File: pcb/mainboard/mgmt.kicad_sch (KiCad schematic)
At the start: 91 parts, among them J10 FAN_01, J11 XILINX_JTAG, J12 JUMPER_0402_SPDT, J13 JUMPER_0402_SPDT, J14 RJ45, J15 PMOD_HOST, J48 CONN_01X10, J8 FAN_01, J9 CONN_01X03, U23 STM32H735-UFBGA176-25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

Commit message: More work in supervisor region
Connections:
- net FAN1_TACH: now also U8.G22 (IO_L8N_T1_D12_14); no longer U8.J21 (IO_L10P_T1_D14_14)
- net FRONTPANEL_CS_N: now also U8.L21 (IO_L18N_T2_A11_D27_14); no longer U8.E21 (IO_L7P_T1_D09_14)
- net FRONTPANEL_MISO: now also U8.N22 (IO_L15P_T2_DQS_RDWR_B_14); no longer U8.H22 (IO_L8P_T1_D11_14)
- net FRONTPANEL_MOSI: now also U8.K21 (IO_L16P_T2_CSI_B_14); no longer U8.E22 (IO_L7N_T1_D10_14)
- net FRONTPANEL_SCK: now also U8.K22 (IO_L16N_T2_A15_D31_14); no longer U8.G22 (IO_L8N_T1_D12_14)
- net MCU_IRQ: now also U8.J21 (IO_L10P_T1_D14_14); no longer U8.M20 (IO_L18P_T2_A12_D28_14)
- net MCU_QSPI_CS_N: now also U8.H22 (IO_L8P_T1_D11_14); no longer U8.M21 (IO_L17N_T2_A13_D29_14)
- net MCU_QSPI_DQ0: now also U8.F20 (IO_L4N_T0_D05_14); no longer U8.L20 (IO_L12N_T1_MRCC_14)
- net MCU_QSPI_DQ1: now also U8.E22 (IO_L7N_T1_D10_14); no longer U8.N22 (IO_L15P_T2_DQS_RDWR_B_14)
- net MCU_QSPI_DQ2: now also U8.G20 (IO_L4P_T0_D04_14); no longer U8.K22 (IO_L16N_T2_A15_D31_14)
- net MCU_QSPI_DQ3: now also U8.F21 (IO_L9N_T1_DQS_D13_14); no longer U8.L21 (IO_L18N_T2_A11_D27_14)
- net MCU_QSPI_SCK: now also U8.E21 (IO_L7P_T1_D09_14); no longer U8.K21 (IO_L16P_T2_CSI_B_14)
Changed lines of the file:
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@@
   (no_connect (at 245.11 60.96))
   (no_connect (at 287.02 91.44))
+  (no_connect (at 354.33 81.28))
   (no_connect (at 280.67 71.12))
-  (no_connect (at 354.33 40.64))
   (no_connect (at 200.66 119.38))
   (no_connect (at 200.66 91.44))
@@
   (no_connect (at 245.11 45.72))
   (no_connect (at 245.11 119.38))
+  (no_connect (at 354.33 109.22))
   (no_connect (at 152.4 111.76))
-  (no_connect (at 354.33 38.1))
   (no_connect (at 287.02 104.14))
   (no_connect (at 354.33 83.82))
@@
   (no_connect (at 280.67 38.1))
   (no_connect (at 354.33 132.08))
+  (no_connect (at 354.33 106.68))
   (no_connect (at 245.11 40.64))
   (no_connect (at 245.11 99.06))
-  (no_connect (at 354.33 66.04))
   (no_connect (at 280.67 35.56))
   (no_connect (at 200.66 101.6))
@@
     (effects (font (size 1.27 1.27)) (justify right bottom))
   )
-  (label "MCU_QSPI_DQ3" (at 354.33 111.76 180)
-    (effects (font (size 1.27 1.27)) (justify right bottom))
-  )
-  (label "FAN1_TACH" (at 354.33 68.58 180)
+  (label "MCU_QSPI_DQ3" (at 354.33 66.04 180)
+    (effects (font (size 1.27 1.27)) (justify right bottom))
+  )
+  (label "FAN1_TACH" (at 354.33 60.96 180)
     (effects (font (size 1.27 1.27)) (justify right bottom))
   )
@@
     (effects (font (size 1.27 1.27)) (justify right bottom))
   )
-  (label "MCU_QSPI_SCK" (at 354.33 99.06 180)
+  (label "MCU_QSPI_SCK" (at 354.33 53.34 180)
     (effects (font (size 1.27 1.27)) (justify right bottom))
   )
@@
     (effects (font (size 1.27 1.27)) (justify right bottom))
   )
-  (label "MCU_QSPI_DQ1" (at 354.33 93.98 180)
+  (label "MCU_QSPI_DQ1" (at 354.33 55.88 180)
     (effects (font (size 1.27 1.27)) (justify right bottom))
   )
@@
     (effects (font (size 1.27 1.27)) (justify left bottom))
   )
-  (label "MCU_QSPI_CS_N" (at 354.33 106.68 180)
+  (label "MCU_QSPI_CS_N" (at 354.33 58.42 180)
     (effects (font (size 1.27 1.27)) (justify right bottom))
   )
@@
     (effects (font (size 1.27 1.27)) (justify left bottom))
   )
-  (label "MCU_QSPI_DQ0" (at 354.33 81.28 180)
+  (label "MCU_QSPI_DQ0" (at 354.33 40.64 180)
     (effects (font (size 1.27 1.27)) (justify right bottom))
   )
@@
     (effects (font (size 1.27 1.27)) (justify right bottom))
   )
-  (label "FRONTPANEL_SCK" (at 354.33 60.96 180)
+  (label "FRONTPANEL_SCK" (at 354.33 101.6 180)
     (effects (font (size 1.27 1.27)) (justify right bottom))
   )
@@
     (effects (font (size 1.27 1.27)) (justify right bottom))
   )
-  (label "FRONTPANEL_MISO" (at 354.33 58.42 180)
+  (label "FRONTPANEL_MISO" (at 354.33 93.98 180)
     (effects (font (size 1.27 1.27)) (justify right bottom))
   )
@@
     (effects (font (size 1.27 1.27)) (justify right bottom))
   )
-  (label "FRONTPANEL_CS_N" (at 354.33 53.34 180)
+  (label "FRONTPANEL_CS_N" (at 354.33 111.76 180)
     (effects (font (size 1.27 1.27)) (justify right bottom))
   )
@@
     (effects (font (size 1.27 1.27)) (justify right bottom))
   )
-  (label "MCU_QSPI_DQ2" (at 354.33 101.6 180)
+  (label "MCU_QSPI_DQ2" (at 354.33 38.1 180)
     (effects (font (size 1.27 1.27)) (justify right bottom))
   )
@@
     (effects (font (size 1.27 1.27)) (justify right bottom))
   )
-  (label "FRONTPANEL_MOSI" (at 354.33 55.88 180)
+  (label "FRONTPANEL_MOSI" (at 354.33 99.06 180)
     (effects (font (size 1.27 1.27)) (justify right bottom))
   )
@@
     (effects (font (size 1.27 1.27)) (justify left bottom))
   )
-  (label "MCU_IRQ" (at 354.33 109.22 180)
-    (effects (font (size 1.27 1.27)) (justify right bottom))
-  )
+  (label "MCU_IRQ" (at 354.33 68.58 180)
+    (effects (font (size 1.27 1.27)) (justify right bottom))
+  )

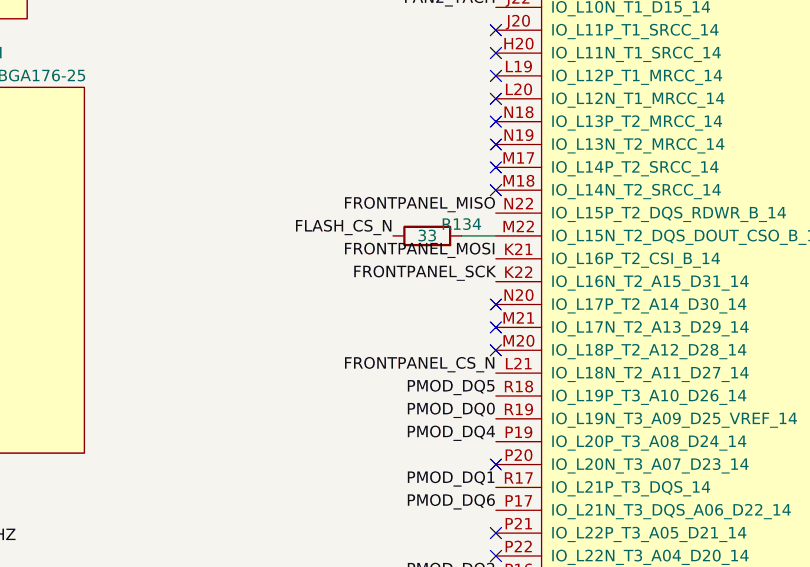
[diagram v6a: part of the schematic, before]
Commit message: Continued layout, started plane fills. Everything routed except 1V8 regulator
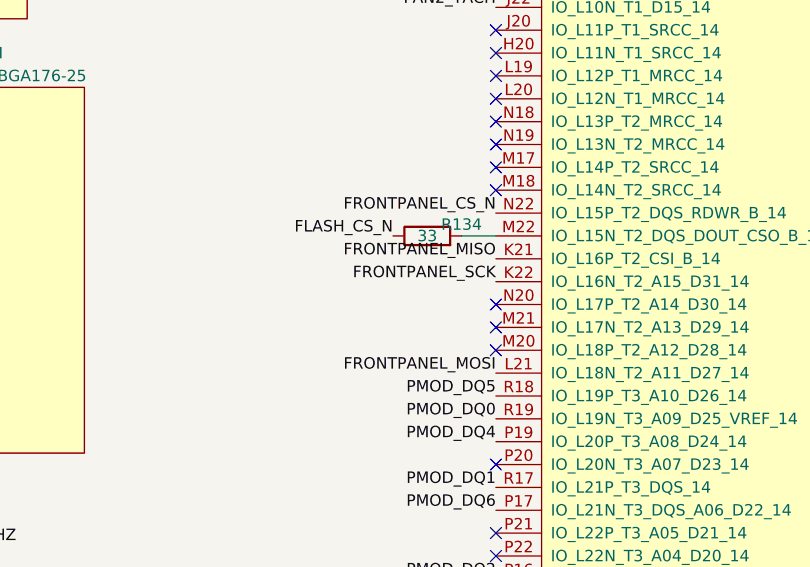
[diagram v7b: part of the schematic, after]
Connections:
- net FRONTPANEL_CS_N: now also U8.N22 (IO_L15P_T2_DQS_RDWR_B_14); no longer U8.L21 (IO_L18N_T2_A11_D27_14)
- net FRONTPANEL_MISO: now also U8.K21 (IO_L16P_T2_CSI_B_14); no longer U8.N22 (IO_L15P_T2_DQS_RDWR_B_14)
- net FRONTPANEL_MOSI: now also U8.L21 (IO_L18N_T2_A11_D27_14); no longer U8.K21 (IO_L16P_T2_CSI_B_14)
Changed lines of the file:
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@@
   (title_block
     (title "Trigger Crossbar")
-    (date "2023-12-22")
+    (date "2023-12-25")
     (rev "0.1")
     (company "Antikernel Labs")
@@
     (effects (font (size 1.27 1.27)) (justify right bottom))
   )
-  (label "FRONTPANEL_MISO" (at 354.33 93.98 180)
+  (label "FRONTPANEL_MISO" (at 354.33 99.06 180)
     (effects (font (size 1.27 1.27)) (justify right bottom))
   )
@@
     (effects (font (size 1.27 1.27)) (justify right bottom))
   )
-  (label "FRONTPANEL_CS_N" (at 354.33 111.76 180)
+  (label "FRONTPANEL_CS_N" (at 354.33 93.98 180)
     (effects (font (size 1.27 1.27)) (justify right bottom))
   )
@@
     (effects (font (size 1.27 1.27)) (justify right bottom))
   )
-  (label "FRONTPANEL_MOSI" (at 354.33 99.06 180)
-    (effects (font (size 1.27 1.27)) (justify right bottom))
-  )
+  (label "FRONTPANEL_MOSI" (at 354.33 111.76 180)
+    (effects (font (size 1.27 1.27)) (justify right bottom))
+  )
